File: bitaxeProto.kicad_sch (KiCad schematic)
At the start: 10 parts, among them J1 XT30

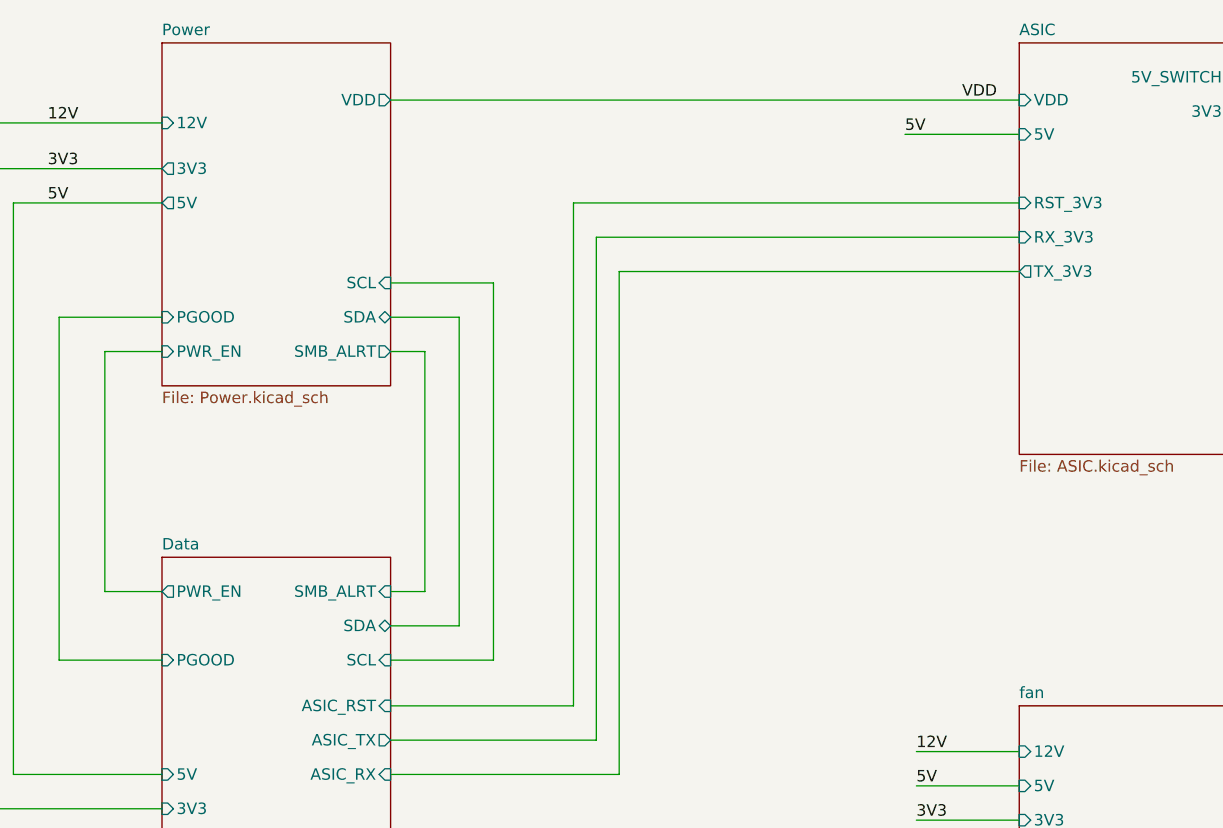
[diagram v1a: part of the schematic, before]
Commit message: add footprints and some 3d cad. rough part placements
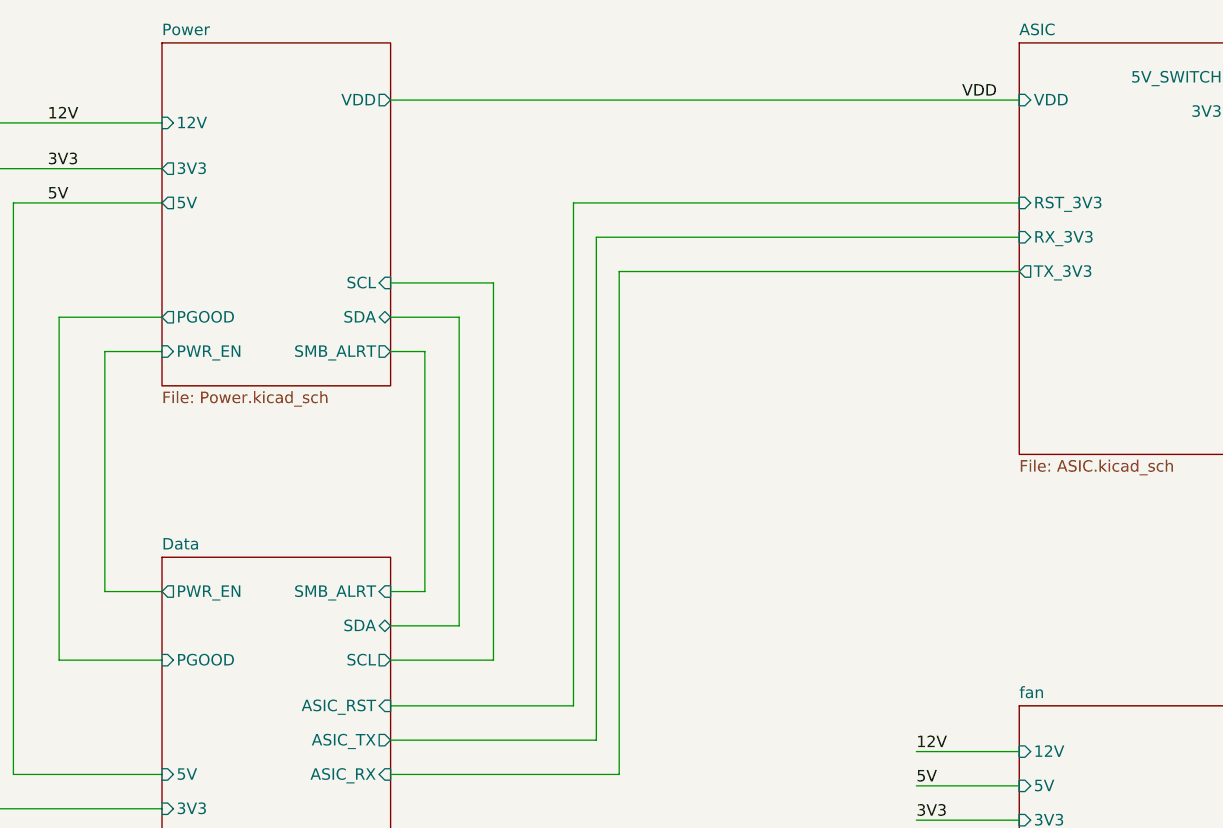
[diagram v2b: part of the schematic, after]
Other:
- sheet ASIC ports: added none; removed 5V

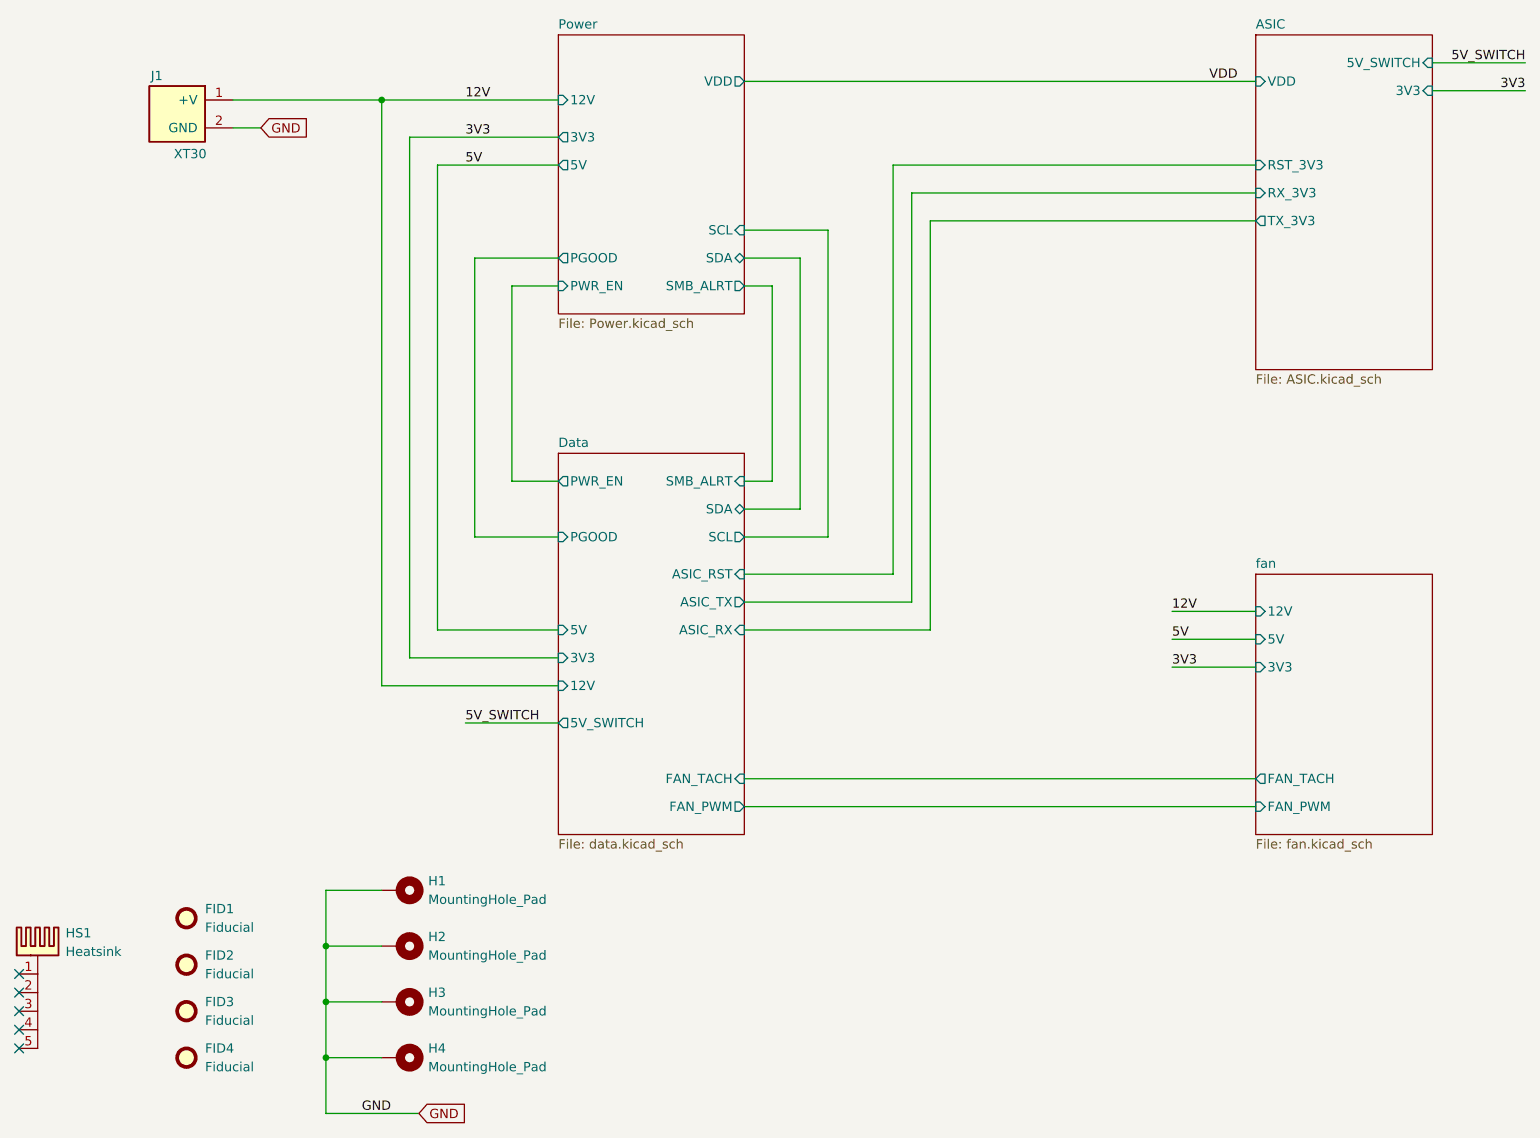
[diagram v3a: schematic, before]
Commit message: update U19 footprint for #1. fix TP silkscreen orientation
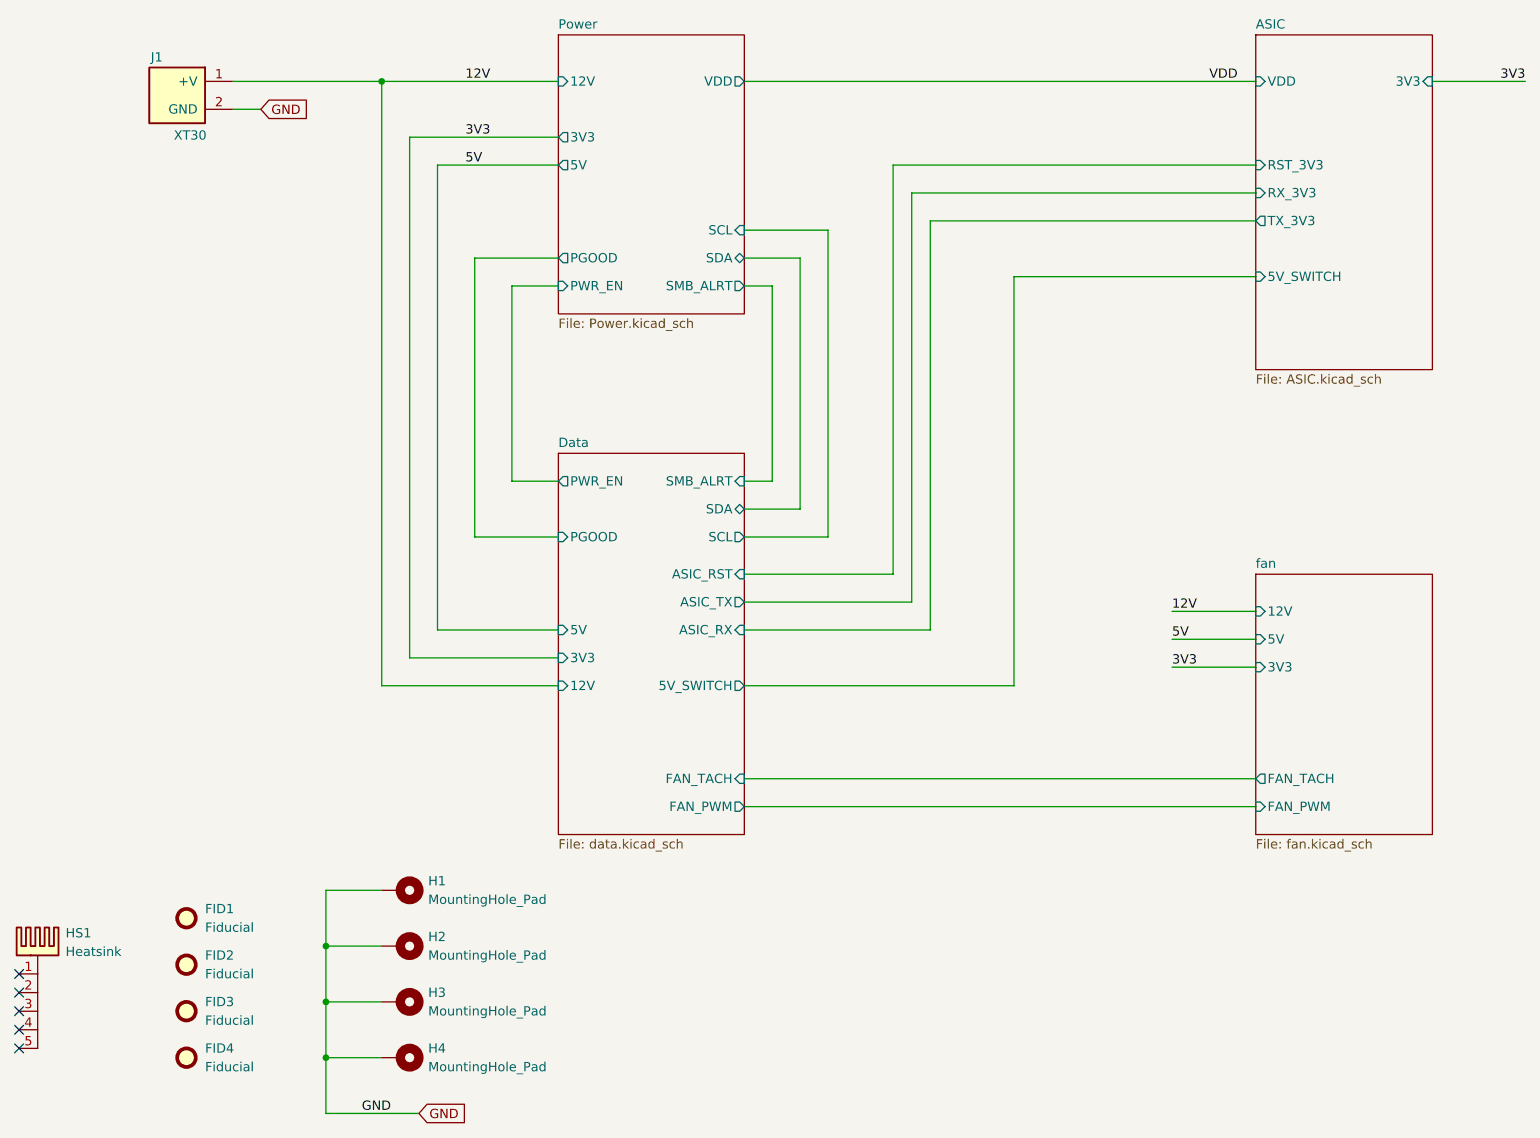
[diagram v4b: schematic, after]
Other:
- moved on the sheet: J1
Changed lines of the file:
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@@
 	)
 	(junction
-		(at 78.74 44.45)
+		(at 78.74 41.91)
 		(diameter 0)
 		(color 0 0 0 0)
@@
 	(wire
 		(pts
-			(xy 222.25 43.18) (xy 234.95 43.18)
+			(xy 222.25 41.91) (xy 234.95 41.91)
 		)
 		(stroke
@@
 	(wire
 		(pts
-			(xy 58.42 44.45) (xy 78.74 44.45)
+			(xy 58.42 41.91) (xy 78.74 41.91)
 		)
 		(stroke
@@
 	(wire
 		(pts
+			(xy 198.12 68.58) (xy 165.1 68.58)
+		)
+		(stroke
+			(width 0)
+			(type default)
+		)
+	)
+	(wire
+		(pts
+			(xy 165.1 124.46) (xy 128.27 124.46)
+		)
+		(stroke
+			(width 0)
+			(type default)
+		)
+	)
+	(wire
+		(pts
 			(xy 128.27 109.22) (xy 148.59 109.22)
 		)
@@
 	(wire
 		(pts
-			(xy 90.17 129.54) (xy 102.87 129.54)
-		)
-		(stroke
-			(width 0)
-			(type default)
-		)
-	)
-	(wire
-		(pts
 			(xy 82.55 120.65) (xy 82.55 49.53)
 		)
@@
 	(wire
 		(pts
+			(xy 165.1 68.58) (xy 165.1 124.46)
+		)
+		(stroke
+			(width 0)
+			(type default)
+		)
+	)
+	(wire
+		(pts
 			(xy 71.12 152.4) (xy 71.12 160.02)
 		)
@@
 	(wire
 		(pts
-			(xy 222.25 39.37) (xy 234.95 39.37)
-		)
-		(stroke
-			(width 0)
-			(type default)
-		)
-	)
-	(wire
-		(pts
 			(xy 102.87 124.46) (xy 78.74 124.46)
 		)
@@
 	(wire
 		(pts
-			(xy 58.42 48.26) (xy 62.23 48.26)
+			(xy 58.42 45.72) (xy 62.23 45.72)
 		)
 		(stroke
@@
 	(wire
 		(pts
-			(xy 78.74 44.45) (xy 102.87 44.45)
+			(xy 78.74 41.91) (xy 102.87 41.91)
 		)
 		(stroke
@@
 	(wire
 		(pts
-			(xy 78.74 124.46) (xy 78.74 44.45)
+			(xy 78.74 41.91) (xy 78.74 124.46)
 		)
 		(stroke
@@
 		)
 	)
-	(label "5V_SWITCH"
-		(at 90.17 129.54 0)
-		(effects
-			(font
-				(size 1.27 1.27)
-			)
-			(justify left bottom)
-		)
-	)
 	(label "3V3"
 		(at 186.69 121.92 0)
@@
 		)
 	)
-	(label "5V_SWITCH"
-		(at 234.95 39.37 180)
+	(label "3V3"
+		(at 234.95 41.91 180)
 		(effects
 			(font
@@
 		)
 	)
-	(label "3V3"
-		(at 234.95 43.18 180)
-		(effects
-			(font
-				(size 1.27 1.27)
-			)
-			(justify right bottom)
-		)
-	)
 	(label "12V"
-		(at 90.17 44.45 0)
+		(at 90.17 41.91 0)
 		(effects
 			(font
@@
 	(global_label "GND"
 		(shape input)
-		(at 62.23 48.26 0)
+		(at 62.23 45.72 0)
 		(fields_autoplaced yes)
 		(effects
@@
 		)
 		(property "Intersheetrefs" "${INTERSHEET_REFS}"
-			(at 69.0857 48.26 0)
+			(at 69.0857 45.72 0)
 			(hide yes)
 			(show_name no)
@@
 	(symbol
 		(lib_id "bitaxe:XT30PW-M")
-		(at 50.8 45.72 0)
+		(at 50.8 43.18 0)
 		(mirror y)
 		(unit 1)
@@
 		(dnp no)
 		(property "Reference" "J1"
-			(at 48.006 41.148 0)
+			(at 48.006 38.608 0)
 			(show_name no)
 			(do_not_autoplace no)
@@
 		)
 		(property "Value" "XT30"
-			(at 52.578 51.816 0)
+			(at 52.578 49.276 0)
 			(show_name no)
 			(do_not_autoplace no)
@@
 		)
 		(property "Footprint" "bitaxe:XT30PW-M"
-			(at 50.546 61.468 0)
+			(at 50.546 58.928 0)
 			(hide yes)
 			(show_name no)
@@
 		)
 		(property "Datasheet" ""
-			(at 45.212 50.8 0)
+			(at 45.212 48.26 0)
 			(hide yes)
 			(show_name no)
@@
 		)
 		(property "Description" ""
-			(at 50.8 45.72 0)
+			(at 50.8 43.18 0)
 			(hide yes)
 			(show_name no)
@@
 		)
 		(property "PARTNO" "XT30PW-M"
-			(at 50.546 59.182 0)
+			(at 50.546 56.642 0)
 			(hide yes)
 			(show_name no)
@@
 		)
 		(property "DK" ""
-			(at 45.212 52.832 0)
+			(at 45.212 50.292 0)
 			(hide yes)
 			(show_name no)
@@
 		)
 		(property "LCSC" "C431092"
-			(at 50.8 45.72 0)
+			(at 50.8 43.18 0)
 			(hide yes)
 			(show_name no)
@@
 		)
 		(property "Manufacturer" ""
-			(at 50.8 45.72 0)
+			(at 50.8 43.18 0)
 			(hide yes)
 			(show_name no)
@@
 		)
 		(property "Sim.Device" ""
-			(at 50.8 45.72 0)
+			(at 50.8 43.18 0)
 			(hide yes)
 			(show_name no)
@@
 		)
 		(property "Sim.Pins" ""
-			(at 50.8 45.72 0)
+			(at 50.8 43.18 0)
 			(hide yes)
 			(show_name no)
@@
 		)
 		(pin "5V_SWITCH" output
-			(at 102.87 129.54 180)
-			(effects
-				(font
-					(size 1.27 1.27)
-				)
-				(justify left)
+			(at 128.27 124.46 0)
+			(effects
+				(font
+					(size 1.27 1.27)
+				)
+				(justify right)
 			)
 		)
@@
 		)
 		(pin "12V" input
-			(at 102.87 44.45 180)
+			(at 102.87 41.91 180)
 			(effects
 				(font
@@
 		)
 		(pin "5V_SWITCH" input
-			(at 222.25 39.37 0)
-			(effects
-				(font
-					(size 1.27 1.27)
-				)
-				(justify right)
+			(at 198.12 68.58 180)
+			(effects
+				(font
+					(size 1.27 1.27)
+				)
+				(justify left)
 			)
 		)
 		(pin "3V3" input
-			(at 222.25 43.18 0)
-			(effects
-				(font
+			(at 222.25 41.91 0)
+			(effects
+				(font
